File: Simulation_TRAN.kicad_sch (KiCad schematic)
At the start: 2 parts

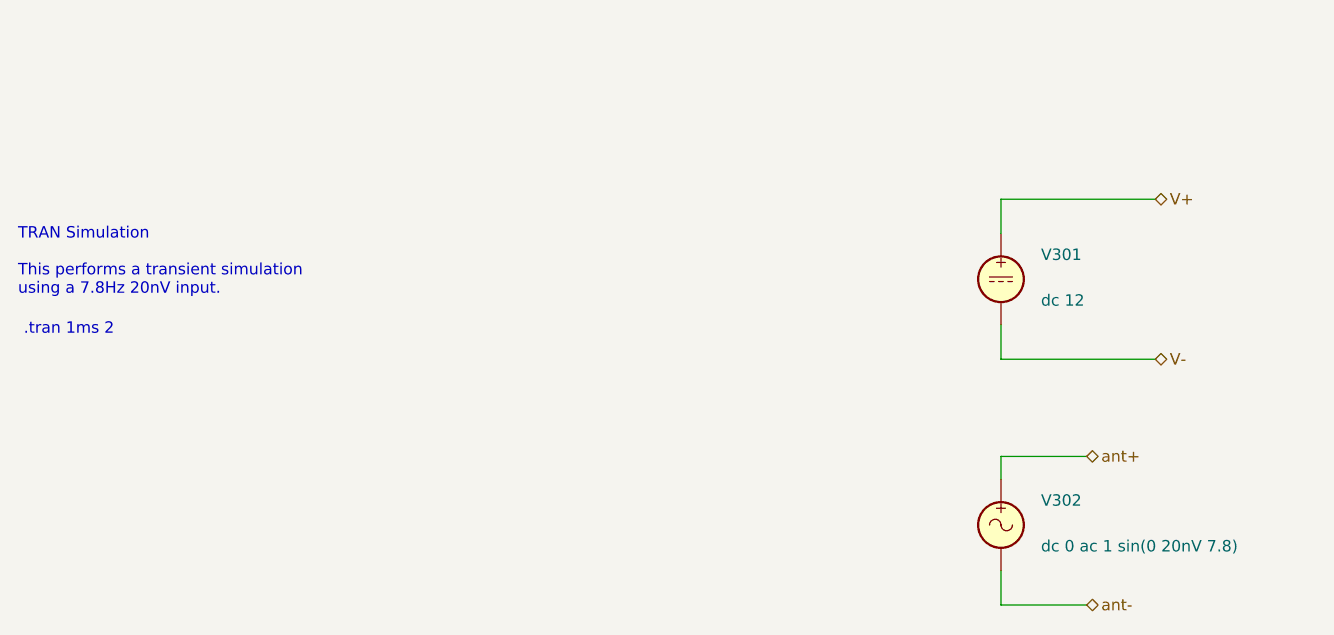
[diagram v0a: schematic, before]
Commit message: Fix simulation primitives and document simulation types
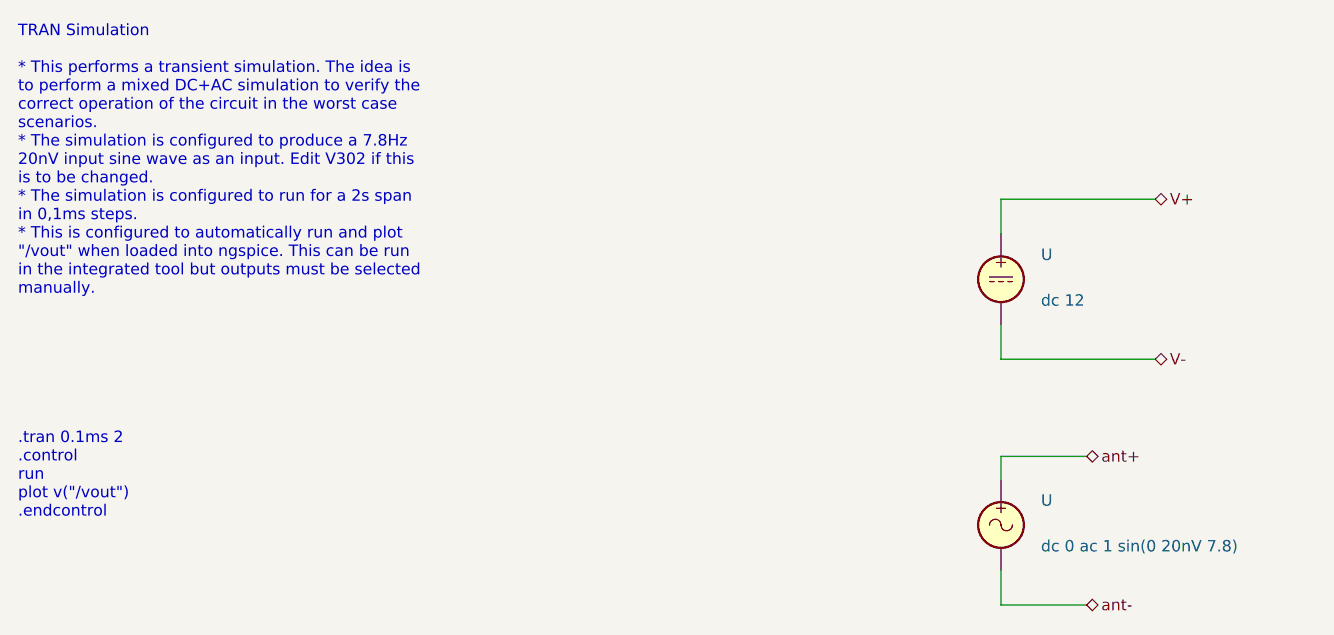
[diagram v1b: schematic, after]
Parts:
- U: renamed from V301; value ~ -> (none)
- U: renamed from V302; value ~ -> (none)
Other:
- note added: ".tran 0.1ms 2 .control run plot v("/vout") .endcontrol"
- note added: "TRAN Simulation * This performs a transient simulation. The idea is to perform a mixed DC+AC simulation to verify the correct operation of the circuit in the worst case scenarios. * The simulation is configured to produce a 7.8Hz 20nV input sine wave as an input. Edit V302 if this is to be changed. * The simulation is configured to run for a 2s span in 0,1ms steps. * This is configured to automat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"
- note removed: ".tran 1ms 2"
- note removed: "TRAN Simulation This performs a transient simulation using a 7.8Hz 20nV input."
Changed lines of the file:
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@@
-(kicad_sch (version 20211123) (generator eeschema)
+(kicad_sch (version 20220404) (generator eeschema)
   (paper "A4")
   (wire (pts (xy 172.72 58.42) (xy 172.72 62.23))
-    (stroke (width 0) (type default) (color 0 0 0 0))
+    (stroke (width 0) (type default))
   )
   (wire (pts (xy 172.72 44.45) (xy 189.865 44.45))
-    (stroke (width 0) (type default) (color 0 0 0 0))
+    (stroke (width 0) (type default))
   )
   (wire (pts (xy 172.72 75.565) (xy 172.72 73.025))
-    (stroke (width 0) (type default) (color 0 0 0 0))
+    (stroke (width 0) (type default))
   )
   (wire (pts (xy 172.72 73.025) (xy 182.245 73.025))
-    (stroke (width 0) (type default) (color 0 0 0 0))
+    (stroke (width 0) (type default))
   )
   (wire (pts (xy 182.245 89.535) (xy 172.72 89.535))
-    (stroke (width 0) (type default) (color 0 0 0 0))
+    (stroke (width 0) (type default))
   )
   (wire (pts (xy 172.72 62.23) (xy 189.865 62.23))
-    (stroke (width 0) (type default) (color 0 0 0 0))
+    (stroke (width 0) (type default))
   )
   (wire (pts (xy 172.72 85.725) (xy 172.72 89.535))
-    (stroke (width 0) (type default) (color 0 0 0 0))
+    (stroke (width 0) (type default))
   )
   (wire (pts (xy 172.72 44.45) (xy 172.72 48.26))
-    (stroke (width 0) (type default) (color 0 0 0 0))
+    (stroke (width 0) (type default))
   )
-  (text "TRAN Simulation\n\nThis performs a transient simulation\nusing a 7.8Hz 20nV input."
+  (text "TRAN Simulation\n\n* This performs a transient simulation. The idea is\nto perform a mixed DC+AC simulation to verify the \ncorrect operation of the circuit in the worst case\nscenarios.\n* The simulation is configured to produce a 7.8Hz\n20nV input sine wave as an input. Edit V302 if this\nis to be changed.\n* The simulation is configured to run for a 2s span\nin 0,1ms steps.\n* This is configured to automatically run and plot\n\"/vout\" when loaded into ngspice. This can be run \nin the integrated tool but outputs must be selected\nmanually."
     (at 63.5 55.245 0)
     (effects (font (size 1.27 1.27)) (justify left bottom))
   )
-  (text ".tran 1ms 2\n" (at 64.135 59.69 0)
+  (text ".tran 0.1ms 2\n.control\nrun\nplot v(\"/vout\")\n.endcontrol"
+    (at 63.5 80.01 0)
     (effects (font (size 1.27 1.27)) (justify left bottom))
   )
-  (hierarchical_label "ant-" (shape bidirectional) (at 182.245 89.535 0)
+  (hierarchical_label "ant-" (shape bidirectional) (at 182.245 89.535 0) (fields_autoplaced)
     (effects (font (size 1.27 1.27)) (justify left))
   )
-  (hierarchical_label "V-" (shape bidirectional) (at 189.865 62.23 0)
+  (hierarchical_label "V-" (shape bidirectional) (at 189.865 62.23 0) (fields_autoplaced)
     (effects (font (size 1.27 1.27)) (justify left))
   )
-  (hierarchical_label "ant+" (shape bidirectional) (at 182.245 73.025 0)
+  (hierarchical_label "ant+" (shape bidirectional) (at 182.245 73.025 0) (fields_autoplaced)
     (effects (font (size 1.27 1.27)) (justify left))
   )
-  (hierarchical_label "V+" (shape bidirectional) (at 189.865 44.45 0)
+  (hierarchical_label "V+" (shape bidirectional) (at 189.865 44.45 0) (fields_autoplaced)
     (effects (font (size 1.27 1.27)) (justify left))
   )
   (symbol (lib_id "Simulation_SPICE:VDC") (at 172.72 53.34 0) (unit 1)
     (in_bom yes) (on_board yes) (fields_autoplaced)
-    (property "Reference" "V301" (id 0) (at 177.165 50.6101 0)
+    (default_instance (reference "U") (unit 1) (value "") (footprint ""))
+    (property "Reference" "U" (id 0) (at 177.165 50.6101 0)
       (effects (font (size 1.27 1.27)) (justify left))
     )
-    (property "Value" "~" (id 1) (at 177.165 53.1501 0)
+    (property "Value" "" (id 1) (at 177.165 53.1501 0)
       (effects (font (size 1.27 1.27)) (justify left))
     )
@@
   (symbol (lib_id "Simulation_SPICE:VSIN") (at 172.72 80.645 0) (unit 1)
     (in_bom yes) (on_board yes) (fields_autoplaced)
-    (property "Reference" "V302" (id 0) (at 177.165 77.9151 0)
+    (default_instance (reference "U") (unit 1) (value "") (footprint ""))
+    (property "Reference" "U" (id 0) (at 177.165 77.9151 0)
       (effects (font (size 1.27 1.27)) (justify left))
     )
-    (property "Value" "~" (id 1) (at 177.165 80.4551 0)
+    (property "Value" "" (id 1) (at 177.165 80.4551 0)
       (effects (font (size 1.27 1.27)) (justify left))
     )
